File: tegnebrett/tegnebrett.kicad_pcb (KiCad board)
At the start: 6 copper layers, 203 parts, among them J1 FH12-45S-0.5SH55, J2 FH12-6S-1SH55, J3 Conn_ST_STDC14, J4 USB-A1HSW6, J5 MCU_Header_Pin, J6 FPGA_debug, J7 FPGA_Header_Pin, J8 DA15_Socket, J9 PJ-002A, SW1 SW_Push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

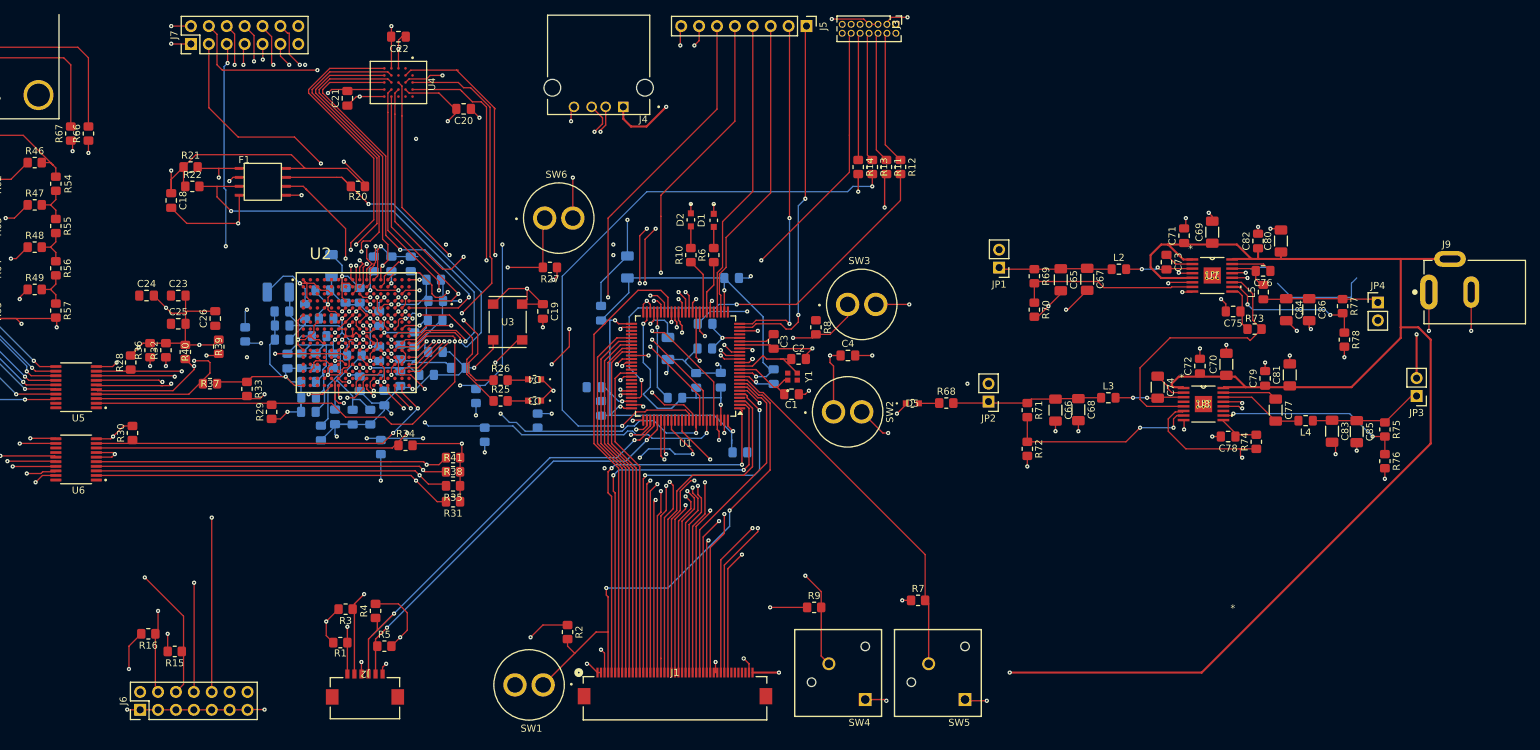
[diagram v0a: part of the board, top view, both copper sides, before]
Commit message: feat: update PCB
Pulled the latest changes from Tormod and imported the EPAD -> 17 fix.
Still, there are some warnings telling us that some footprints have pins
which are not present on the symbols.
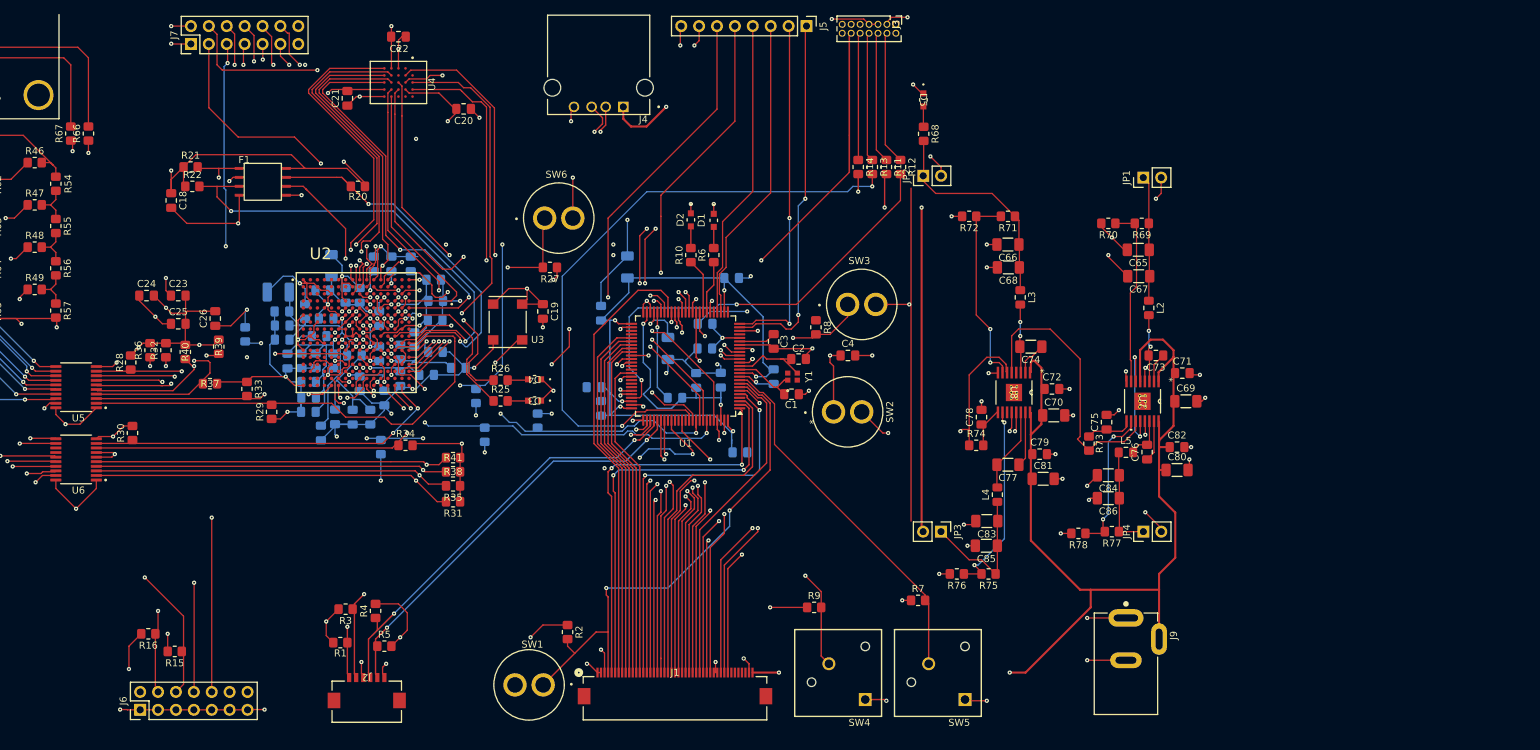
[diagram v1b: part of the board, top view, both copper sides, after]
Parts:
- moved JP3 70.2 mm to (168.8, 85.5), turned to -90 degrees
- moved J9 63.2 mm to (195.0, 97.8), turned to -90 degrees
- moved R76 62.8 mm to (171.0, 91.5), turned to 180 degrees
- moved R75 59.9 mm to (175.5, 91.5), turned to 180 degrees
- moved C85 55.0 mm to (175.2, 87.5), turned to 180 degrees
- moved C83 50.6 mm to (175.2, 84.0), turned to 180 degrees
- moved R78 46.7 mm to (188.2, 85.8), turned to 180 degrees
- moved JP4 46.5 mm to (197.5, 85.5), turned to 90 degrees
- moved R77 45.8 mm to (193.0, 85.5), turned to 180 degrees
- moved L4 45.0 mm to (176.8, 80.2), turned to 90 degrees
- moved D5 43.1 mm to (166.2, 24.2), turned to -90 degrees
- moved R74 39.8 mm to (173.8, 73.2), turned to 0 degrees
- moved C86 39.1 mm to (192.5, 80.8), turned to 180 degrees
- moved C77 38.8 mm to (178.2, 76.0), turned to 180 degrees
- moved R68 38.3 mm to (166.3, 29.0), turned to -90 degrees
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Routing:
- net +3V3: track 982.0 -> 1084.1 mm, vias 48 -> 51
- net POWER_IN: track 244.4 -> 171.2 mm
- net +5V: track 136.9 -> 100.3 mm
- net +1V0: track 171.3 -> 199.9 mm, vias 5 -> 6
- net /DEBUG_JTRST: track 76.8 -> 96.2 mm
- net +1V8: track 188.7 -> 175.5 mm, vias 3 -> 4
- net Net-(JP2-A): track 21.5 -> 31.6 mm
- net /DEBUG_SWCLK: track 97.2 -> 103.6 mm
- net /DEBUG_JTDI: track 96.6 -> 102.8 mm
- net Net-(JP3-A): track 16.4 -> 20.6 mm
- net GND: track 569.8 -> 573.5 mm, vias 98 -> 99
- net Net-(U7-EN2): track 20.1 -> 17.2 mm
- net Net-(U7-SW1): track 12.0 -> 9.68 mm
- net Net-(JP1-A): track 16.2 -> 17.9 mm
- net Net-(JP4-A): track 16.5 -> 14.8 mm
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
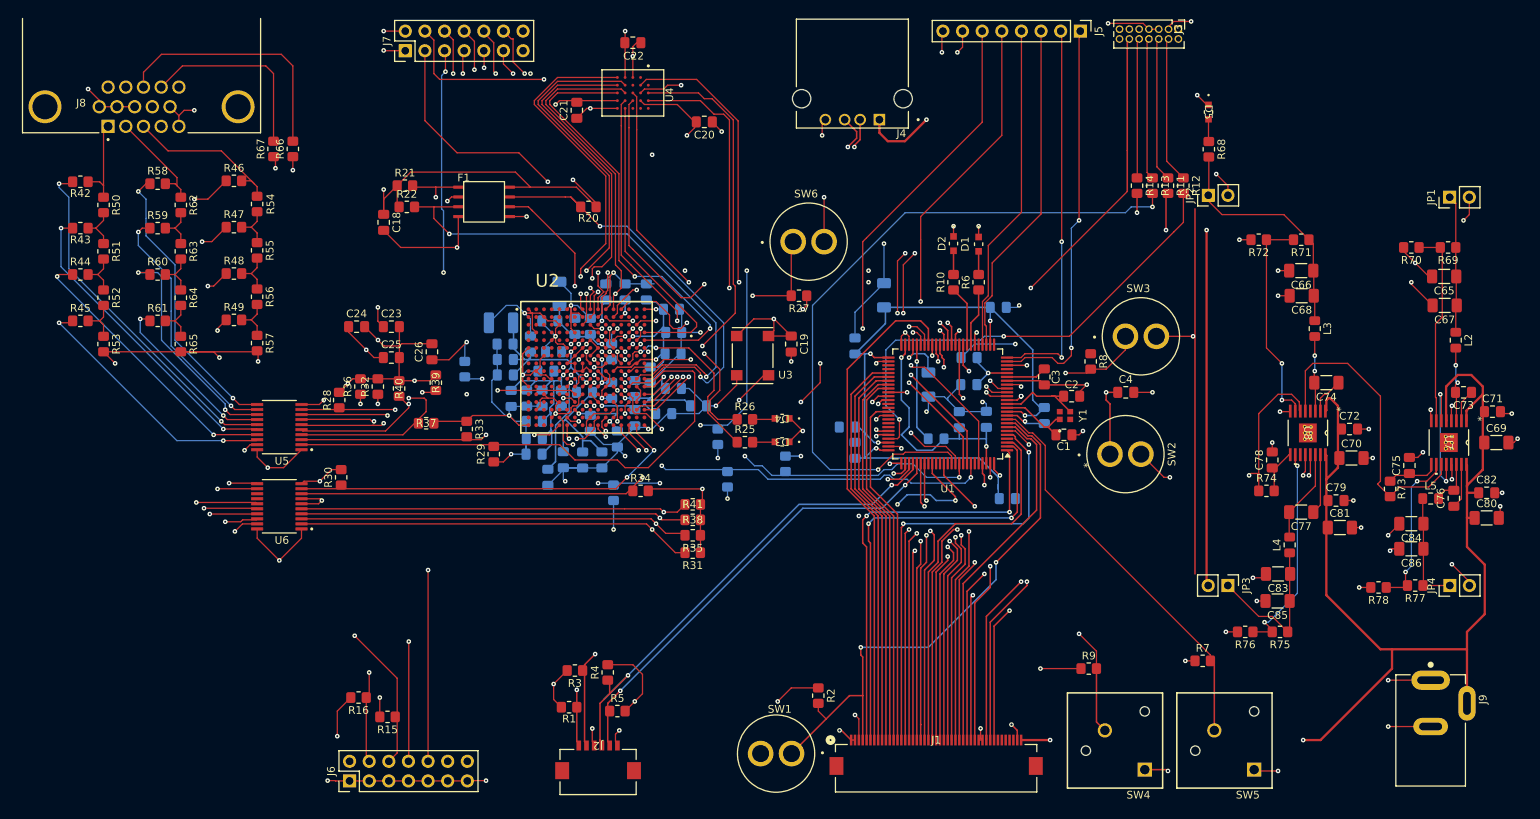
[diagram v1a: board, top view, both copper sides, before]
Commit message: feat: PCB good first version
We've completed something. There are a lot of errors in the PCB related
to the power transformers which are taking in 15V and converting it
down.
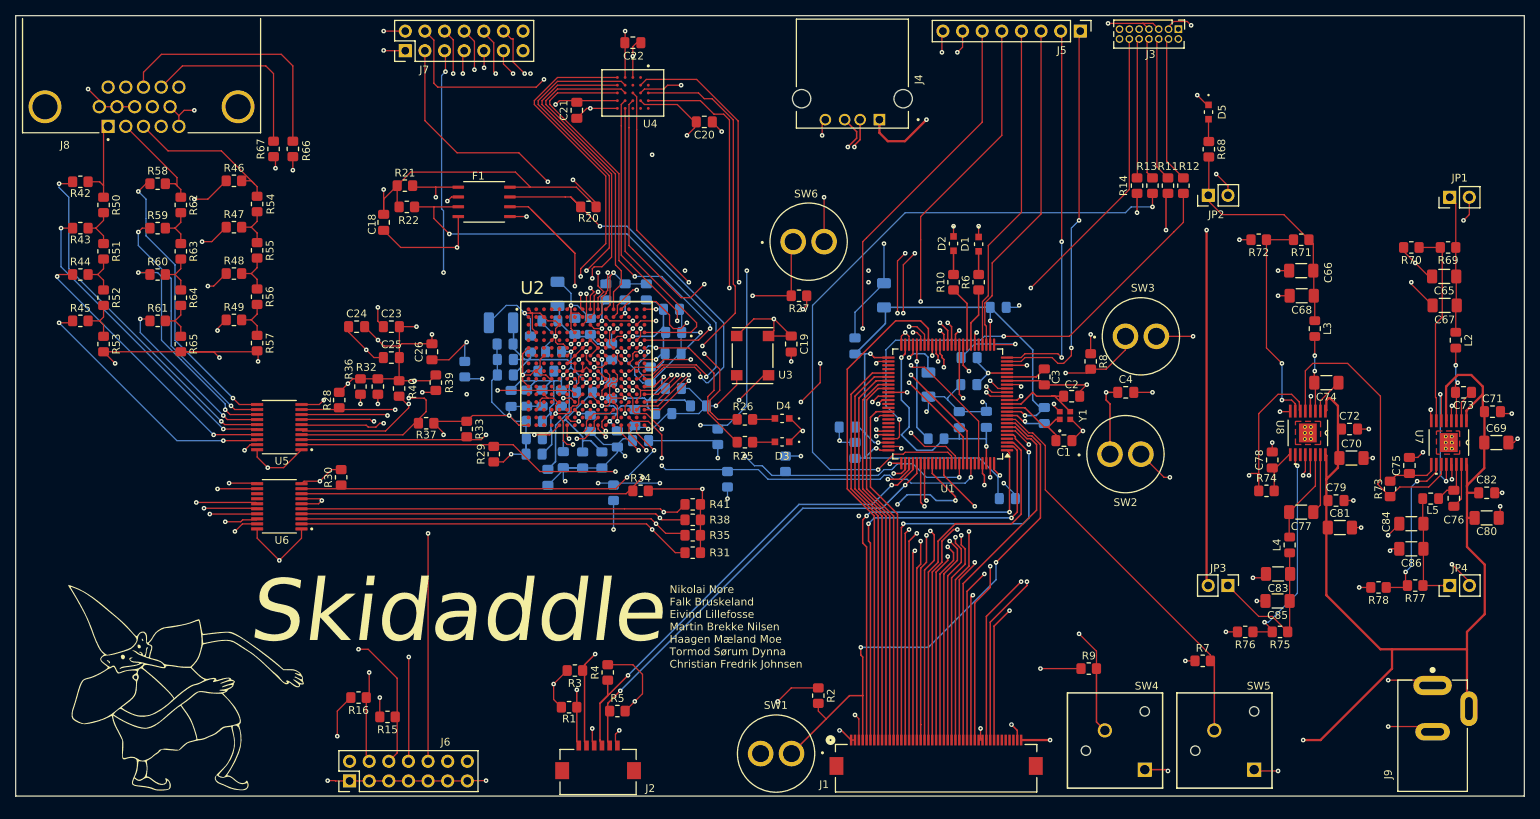
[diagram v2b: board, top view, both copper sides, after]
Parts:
- added G***: LOGO, tegnebrett_modules:skidaddle-logo, F.Cu at (34.0, 98.8)
- moved C37 6.79 mm to (92.8, 66.8), turned to 180 degrees
- moved C1 0.75 mm to (147.5, 66.8)
- moved J9 0.73 mm to (195.2, 98.4)
- moved C31 0.25 mm to (82.0, 47.8)
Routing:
- net +3V3: track 1084.1 -> 1151.6 mm, vias 51 -> 53
- net GND: track 573.5 -> 612.8 mm, vias 99 -> 108
- net /DEBUG_JTRST: track 96.2 -> 77.1 mm
- net Net-(F1-SCLK): track 23.7 -> 31.5 mm
- net /FPGA/VGA/R0: track 70.3 -> 65.9 mm, vias 0 -> 2
- net +5V: track 100.3 -> 97.7 mm
- net /TOUCH_WAKE: track 65.1 -> 62.6 mm
- net /FPGA/Header1: track 66.1 -> 67.6 mm
- net /FPGA/VGA/B2: track 77.4 -> 78.8 mm
- net /FPGA/VGA/B1: track 76.5 -> 77.9 mm
- net /FPGA/VGA/B0: track 76.7 -> 78.1 mm
- net +1V0: track 199.9 -> 201.1 mm
- net /DONE: track 62.8 -> 61.7 mm
- net Net-(U2C-TDO_0): track 58.4 -> 59.3 mm
- net Net-(U1-PH0): track 9.69 -> 10.4 mm
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- added copper zone on F.Cu, net GND
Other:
- board outline added: 195.2 x 101 mm
- board text added: "Nikolai Nore Falk Bruskeland Eivind Lillefosse Martin Brekke Nilsen Haagen Mæland Moe Tormod Sørum Dynna Christian Fredrik Johnsen"
- board text added: "Skidaddle"

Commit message: feat: PCB updates
Latest stuff from Tormod.
We still have 77 Errors and 2 warnings, but we'll ship this!
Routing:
- net +3V3: track 1151.6 -> 420.5 mm
- net GND: track 612.8 -> 614.1 mm
- added copper zone on In4.Cu, net +3V3
